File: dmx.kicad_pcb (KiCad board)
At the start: 4 copper layers, 66 x 18 mm, 41 parts, among them J101 SJ2-25504B-SMT-TR, J102 CORTEX-DEBUG, J103 JAE_DX07S016JA1R1500, SW101 SW_Push, SW102 SW_Push, U101 LTC2851xDD, U102 ATSAMD51G, U103 AP2112K-3.3, Y101 32.768kHz

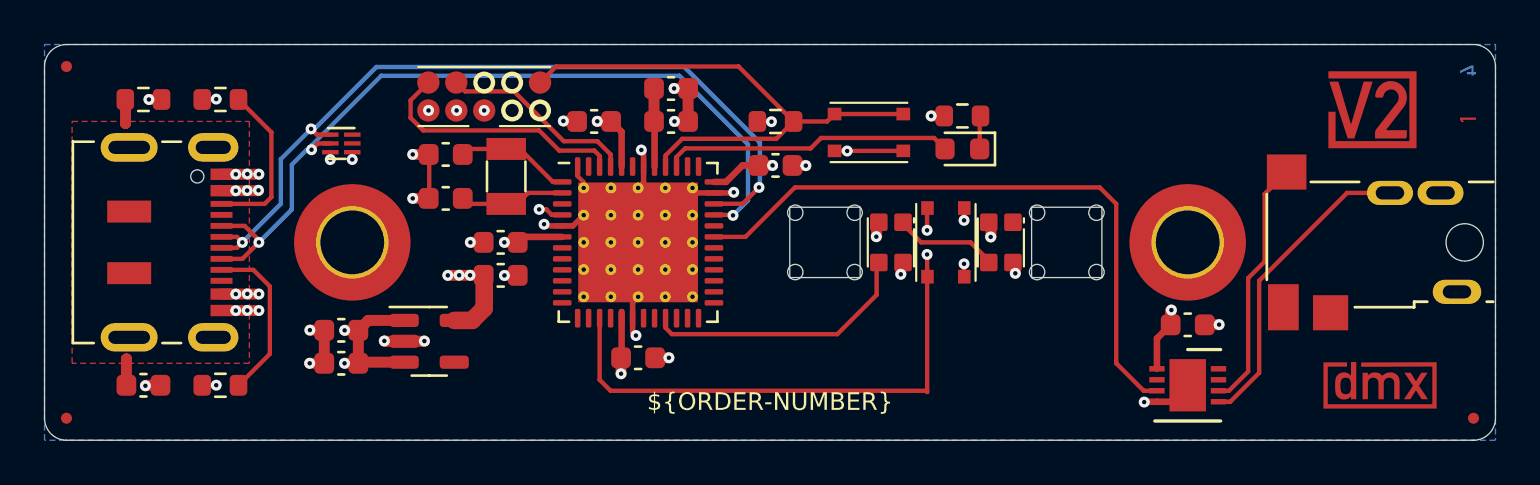
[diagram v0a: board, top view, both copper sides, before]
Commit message: Update to KiCad 7.0
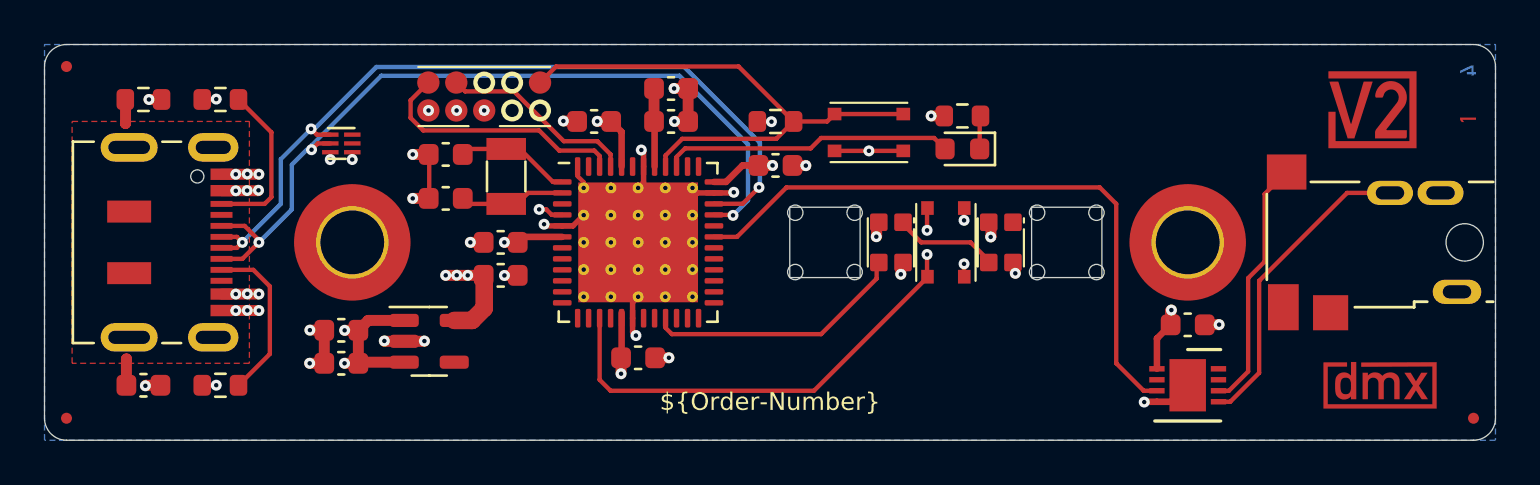
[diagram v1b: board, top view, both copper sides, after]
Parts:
- J103: value JAE_DX07S016JA1R1500 -> JAE_DX07S016JA3; footprint V2_Connector_USB:JAE_DX07S016JA1R1500 -> V2_Connector_USB:JAE_DX07S016JA3
- SPACER101, SPACER102: value 977?2434030 -> 3mm
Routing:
- net /Button: track 26.3 -> 23.2 mm
